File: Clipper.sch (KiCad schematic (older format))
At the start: 35 parts, among them U16 LM4562, U17 LM4562, U18 LM4562

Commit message: More components specified
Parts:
- removed U16, U17, U18: LM4562, ~, symbol LM4562
- added U15, U16: LME49740, ~, symbol LME49740
- D16, D17, D18, D19, D20, D21, D22, D23: DigiKey (none) -> 568-1360-1-ND
- gave numbers to parts that had none: 17
- renumbered C38 to C40, C39 to C41, C40 to C42, C41 to C43
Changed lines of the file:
@@
 Sheet 5 6
 Title ""
-Date "23 may 2014"
+Date "25 may 2014"
 Rev ""
 Comp ""
@@
 	-1   0    0    1
 $EndComp
-$Comp
-L LM4562 U16
-U 1 1 536E7276
-P 2500 3150
-F 0 "U16" H 2750 3000 60  0000 L CNN
-F 1 "LM4562" H 2750 2900 60  0000 L CNN
-F 2 "~" H 2600 3150 60  0000 C CNN
-F 3 "~" H 2600 3150 60  0000 C CNN
-	1    2500 3150
-	1    0    0    -1
-$EndComp
 Text HLabel 2000 3350 3    60   Input ~ 0
 AGND
@@
 F 2 "~" H 2600 2550 60  0000 C CNN
 F 3 "~" H 2600 2550 60  0000 C CNN
+F 4 "568-1360-1-ND" H 2600 2550 60  0001 C CNN "DigiKey"
 	1    2600 2550
 	1    0    0    -1
@@
 F 2 "~" H 2900 2250 60  0000 C CNN
 F 3 "~" H 2900 2250 60  0000 C CNN
+F 4 "568-1360-1-ND" H 2900 2250 60  0001 C CNN "DigiKey"
 	1    2900 2250
 	-1   0    0    -1
@@
 Text HLabel 1850 2350 0    60   Input ~ 0
 +15V
-$Comp
-L LM4562 U16
-U 2 1 536E79AB
-P 2500 5050
-F 0 "U16" H 2750 4900 60  0000 L CNN
-F 1 "LM4562" H 2750 4800 60  0000 L CNN
-F 2 "~" H 2600 5050 60  0000 C CNN
-F 3 "~" H 2600 5050 60  0000 C CNN
-	2    2500 5050
-	1    0    0    -1
-$EndComp
 Text HLabel 2000 5250 3    60   Input ~ 0
 AGND
@@
 F 2 "~" H 2600 4450 60  0000 C CNN
 F 3 "~" H 2600 4450 60  0000 C CNN
+F 4 "568-1360-1-ND" H 2600 4450 60  0001 C CNN "DigiKey"
 	1    2600 4450
 	1    0    0    -1
@@
 F 2 "~" H 2900 4150 60  0000 C CNN
 F 3 "~" H 2900 4150 60  0000 C CNN
+F 4 "568-1360-1-ND" H 2900 4150 60  0001 C CNN "DigiKey"
 	1    2900 4150
 	-1   0    0    -1
@@
 Text HLabel 1850 5650 0    60   Input ~ 0
 -15V
-$Comp
-L LM4562 U17
-U 1 1 536E7B83
-P 4650 3800
-F 0 "U17" H 4900 3650 60  0000 L CNN
-F 1 "LM4562" H 4900 3550 60  0000 L CNN
-F 2 "~" H 4750 3800 60  0000 C CNN
-F 3 "~" H 4750 3800 60  0000 C CNN
-	1    4650 3800
-	1    0    0    -1
-$EndComp
 Text HLabel 4150 4000 3    60   Input ~ 0
 AGND
@@
 Text HLabel 4650 4200 0    60   Input ~ 0
 -15V
-$Comp
-L LM4562 U17
-U 2 1 536E8363
-P 7900 3150
-F 0 "U17" H 8150 3000 60  0000 L CNN
-F 1 "LM4562" H 8150 2900 60  0000 L CNN
-F 2 "~" H 8000 3150 60  0000 C CNN
-F 3 "~" H 8000 3150 60  0000 C CNN
-	2    7900 3150
-	1    0    0    -1
-$EndComp
 Text HLabel 7400 3350 3    60   Input ~ 0
 AGND
@@
 F 2 "~" H 8000 2550 60  0000 C CNN
 F 3 "~" H 8000 2550 60  0000 C CNN
+F 4 "568-1360-1-ND" H 8000 2550 60  0001 C CNN "DigiKey"
 	1    8000 2550
 	1    0    0    -1
@@
 F 2 "~" H 8300 2250 60  0000 C CNN
 F 3 "~" H 8300 2250 60  0000 C CNN
+F 4 "568-1360-1-ND" H 8300 2250 60  0001 C CNN "DigiKey"
 	1    8300 2250
 	-1   0    0    -1
@@
 Text HLabel 7250 2350 0    60   Input ~ 0
 +15V
-$Comp
-L LM4562 U18
-U 1 1 536E839D
-P 7900 5050
-F 0 "U18" H 8150 4900 60  0000 L CNN
-F 1 "LM4562" H 8150 4800 60  0000 L CNN
-F 2 "~" H 8000 5050 60  0000 C CNN
-F 3 "~" H 8000 5050 60  0000 C CNN
-	1    7900 5050
-	1    0    0    -1
-$EndComp
 Text HLabel 7400 5250 3    60   Input ~ 0
 AGND
@@
 F 2 "~" H 8000 4450 60  0000 C CNN
 F 3 "~" H 8000 4450 60  0000 C CNN
+F 4 "568-1360-1-ND" H 8000 4450 60  0001 C CNN "DigiKey"
 	1    8000 4450
 	1    0    0    -1
@@
 F 2 "~" H 8300 4150 60  0000 C CNN
 F 3 "~" H 8300 4150 60  0000 C CNN
+F 4 "568-1360-1-ND" H 8300 4150 60  0001 C CNN "DigiKey"
 	1    8300 4150
 	-1   0    0    -1
@@
 Text HLabel 7250 5650 0    60   Input ~ 0
 -15V
-$Comp
-L LM4562 U18
-U 2 1 536E83E9
-P 10050 3800
-F 0 "U18" H 10300 3650 60  0000 L CNN
-F 1 "LM4562" H 10300 3550 60  0000 L CNN
-F 2 "~" H 10150 3800 60  0000 C CNN
-F 3 "~" H 10150 3800 60  0000 C CNN
-	2    10050 3800
-	1    0    0    -1
-$EndComp
 Text HLabel 9550 4000 3    60   Input ~ 0
 AGND
@@
 Set to clip at +/- 6.25 V
 $Comp
-L C C38
+L C C40
 U 1 1 536EC1E0
 P 5450 1700
-F 0 "C38" H 5450 1800 40  0000 L CNN
+F 0 "C40" H 5450 1800 40  0000 L CNN
 F 1 "470n" H 5456 1615 40  0000 L CNN
 F 2 "~" H 5488 1550 30  0000 C CNN
@@
 $EndComp
 $Comp
-L C C40
+L C C42
 U 1 1 537D7769
 P 5800 1700
-F 0 "C40" H 5800 1800 40  0000 L CNN
+F 0 "C42" H 5800 1800 40  0000 L CNN
 F 1 "470n" H 5806 1615 40  0000 L CNN
 F 2 "~" H 5838 1550 30  0000 C CNN
@@
 $EndComp
 $Comp
-L C C39
+L C C41
 U 1 1 537D7778
 P 5450 2100
-F 0 "C39" H 5450 2200 40  0000 L CNN
+F 0 "C41" H 5450 2200 40  0000 L CNN
 F 1 "470n" H 5456 2015 40  0000 L CNN
 F 2 "~" H 5488 1950 30  0000 C CNN
@@
 $EndComp
 $Comp
-L C C41
+L C C43
 U 1 1 537D7787
 P 5800 2100
-F 0 "C41" H 5800 2200 40  0000 L CNN
+F 0 "C43" H 5800 2200 40  0000 L CNN
 F 1 "470n" H 5806 2015 40  0000 L CNN
 F 2 "~" H 5838 1950 30  0000 C CNN
@@
 $EndComp
 $Comp
-L R R?
+L R R34
 U 1 1 537F3861
 P 1850 5400
-F 0 "R?" V 1930 5400 40  0000 C CNN
+F 0 "R34" V 1930 5400 40  0000 C CNN
 F 1 "24k" V 1857 5401 40  0000 C CNN
 F 2 "~" V 1780 5400 30  0000 C CNN
@@
 $EndComp
 $Comp
-L R R?
+L R R44
 U 1 1 537F3868
 P 7250 5400
-F 0 "R?" V 7330 5400 40  0000 C CNN
+F 0 "R44" V 7330 5400 40  0000 C CNN
 F 1 "24k" V 7257 5401 40  0000 C CNN
 F 2 "~" V 7180 5400 30  0000 C CNN
@@
 $EndComp
 $Comp
-L R R?
+L R R43
 U 1 1 537F387B
 P 7250 2600
-F 0 "R?" V 7330 2600 40  0000 C CNN
+F 0 "R43" V 7330 2600 40  0000 C CNN
 F 1 "24k" V 7257 2601 40  0000 C CNN
 F 2 "~" V 7180 2600 30  0000 C CNN
@@
 $EndComp
 $Comp
-L R R?
+L R R32
 U 1 1 537F38E5
 P 1450 4950
-F 0 "R?" V 1530 4950 40  0000 C CNN
+F 0 "R32" V 1530 4950 40  0000 C CNN
 F 1 "10k" V 1450 4950 40  0000 C CNN
 F 2 "~" V 1380 4950 30  0000 C CNN
@@
 $EndComp
 $Comp
-L R R?
+L R R42
 U 1 1 537F38EC
 P 6850 4950
-F 0 "R?" V 6930 4950 40  0000 C CNN
+F 0 "R42" V 6930 4950 40  0000 C CNN
 F 1 "10k" V 6850 4950 40  0000 C CNN
 F 2 "~" V 6780 4950 30  0000 C CNN
@@
 $EndComp
 $Comp
-L R R?
+L R R41
 U 1 1 537F38F3
 P 6850 3050
-F 0 "R?" V 6930 3050 40  0000 C CNN
+F 0 "R41" V 6930 3050 40  0000 C CNN
 F 1 "10k" V 6850 3050 40  0000 C CNN
 F 2 "~" V 6780 3050 30  0000 C CNN
@@
 $EndComp
 $Comp
-L R R?
+L R R35
 U 1 1 537F38FA
 P 2350 2250
-F 0 "R?" V 2430 2250 40  0000 C CNN
+F 0 "R35" V 2430 2250 40  0000 C CNN
 F 1 "10k" V 2350 2250 40  0000 C CNN
 F 2 "~" V 2280 2250 30  0000 C CNN
@@
 $EndComp
 $Comp
-L R R?
+L R R36
 U 1 1 537F3901
 P 2350 4150
-F 0 "R?" V 2430 4150 40  0000 C CNN
+F 0 "R36" V 2430 4150 40  0000 C CNN
 F 1 "10k" V 2350 4150 40  0000 C CNN
 F 2 "~" V 2280 4150 30  0000 C CNN
@@
 $EndComp
 $Comp
-L R R?
+L R R45
 U 1 1 537F3908
 P 7750 2250
-F 0 "R?" V 7830 2250 40  0000 C CNN
+F 0 "R45" V 7830 2250 40  0000 C CNN
 F 1 "10k" V 7750 2250 40  0000 C CNN
 F 2 "~" V 7680 2250 30  0000 C CNN
@@
 $EndComp
 $Comp
-L R R?
+L R R46
 U 1 1 537F390F
 P 7750 4150
-F 0 "R?" V 7830 4150 40  0000 C CNN
+F 0 "R46" V 7830 4150 40  0000 C CNN
 F 1 "10k" V 7750 4150 40  0000 C CNN
 F 2 "~" V 7680 4150 30  0000 C CNN
@@
 $EndComp
 $Comp
-L R R?
+L R R48
 U 1 1 537F3ABF
 P 9000 3700
-F 0 "R?" V 9080 3700 40  0000 C CNN
+F 0 "R48" V 9080 3700 40  0000 C CNN
 F 1 "2.2k" V 9007 3701 40  0000 C CNN
 F 2 "~" V 8930 3700 30  0000 C CNN
@@
 $EndComp
 $Comp
-L R R?
+L R R49
 U 1 1 537F3AC6
 P 9000 4000
-F 0 "R?" V 9080 4000 40  0000 C CNN
+F 0 "R49" V 9080 4000 40  0000 C CNN
 F 1 "2.2k" V 9007 4001 40  0000 C CNN
 F 2 "~" V 8930 4000 30  0000 C CNN
@@
 $EndComp
 $Comp
-L R R?
+L R R50
 U 1 1 537F3ACD
 P 10150 3200
-F 0 "R?" V 10230 3200 40  0000 C CNN
+F 0 "R50" V 10230 3200 40  0000 C CNN
 F 1 "2.2k" V 10157 3201 40  0000 C CNN
 F 2 "~" V 10080 3200 30  0000 C CNN
@@
 $EndComp
 $Comp
-L R R?
+L R R37
 U 1 1 537F3AD4
 P 3600 3400
-F 0 "R?" V 3680 3400 40  0000 C CNN
+F 0 "R37" V 3680 3400 40  0000 C CNN
 F 1 "2.2k" V 3607 3401 40  0000 C CNN
 F 2 "~" V 3530 3400 30  0000 C CNN
@@
 $EndComp
 $Comp
-L R R?
+L R R38
 U 1 1 537F3ADB
 P 3600 3700
-F 0 "R?" V 3680 3700 40  0000 C CNN
+F 0 "R38" V 3680 3700 40  0000 C CNN
 F 1 "2.2k" V 3607 3701 40  0000 C CNN
 F 2 "~" V 3530 3700 30  0000 C CNN
@@
 $EndComp
 $Comp
-L R R?
+L R R39
 U 1 1 537F3AE2
 P 3600 4000
-F 0 "R?" V 3680 4000 40  0000 C CNN
+F 0 "R39" V 3680 4000 40  0000 C CNN
 F 1 "2.2k" V 3607 4001 40  0000 C CNN
 F 2 "~" V 3530 4000 30  0000 C CNN
@@
 $EndComp
 $Comp
-L R R?
+L R R40
 U 1 1 537F3AE9
 P 4750 3200
-F 0 "R?" V 4830 3200 40  0000 C CNN
+F 0 "R40" V 4830 3200 40  0000 C CNN
 F 1 "2.2k" V 4757 3201 40  0000 C CNN
 F 2 "~" V 4680 3200 30  0000 C CNN
@@
 	0    -1   -1   0
 $EndComp
+$Comp
+L LME49740 U15
+U 3 1 5380327C
+P 2500 3150
+F 0 "U15" H 2750 3000 60  0000 L CNN
+F 1 "LME49740" H 2750 2900 60  0000 L CNN
+F 2 "~" H 2600 3150 60  0000 C CNN
+F 3 "~" H 2600 3150 60  0000 C CNN
+	3    2500 3150
+	1    0    0    -1
+$EndComp
+$Comp
+L LME49740 U15
+U 4 1 53803307
+P 2500 5050
+F 0 "U15" H 2750 4900 60  0000 L CNN
+F 1 "LME49740" H 2750 4800 60  0000 L CNN
+F 2 "~" H 2600 5050 60  0000 C CNN
+F 3 "~" H 2600 5050 60  0000 C CNN
+	4    2500 5050
+	1    0    0    -1
+$EndComp
+$Comp
+L LME49740 U16
+U 4 1 53803335
+P 7900 5050
+F 0 "U16" H 8150 4900 60  0000 L CNN
+F 1 "LME49740" H 8150 4800 60  0000 L CNN
+F 2 "~" H 8000 5050 60  0000 C CNN
+F 3 "~" H 8000 5050 60  0000 C CNN
+	4    7900 5050
+	1    0    0    -1
+$EndComp
+$Comp
+L LME49740 U16
+U 3 1 5380334C
+P 7900 3150
+F 0 "U16" H 8150 3000 60  0000 L CNN
+F 1 "LME49740" H 8150 2900 60  0000 L CNN
+F 2 "~" H 8000 3150 60  0000 C CNN
+F 3 "~" H 8000 3150 60  0000 C CNN
+	3    7900 3150
+	1    0    0    -1
+$EndComp
+$Comp
+L LME49740 U15
+U 2 1 538036F5
+P 4650 3800
+F 0 "U15" H 4900 3650 60  0000 L CNN
+F 1 "LME49740" H 4900 3550 60  0000 L CNN
+F 2 "~" H 4750 3800 60  0000 C CNN
+F 3 "~" H 4750 3800 60  0000 C CNN
+	2    4650 3800
+	1    0    0    -1
+$EndComp
+$Comp
+L LME49740 U16
+U 2 1 5380372A
+P 10050 3800
+F 0 "U16" H 10300 3650 60  0000 L CNN
+F 1 "LME49740" H 10300 3550 60  0000 L CNN
+F 2 "~" H 10150 3800 60  0000 C CNN
+F 3 "~" H 10150 3800 60  0000 C CNN
+	2    10050 3800
+	1    0    0    -1
+$EndComp
 $EndSCHEMATC

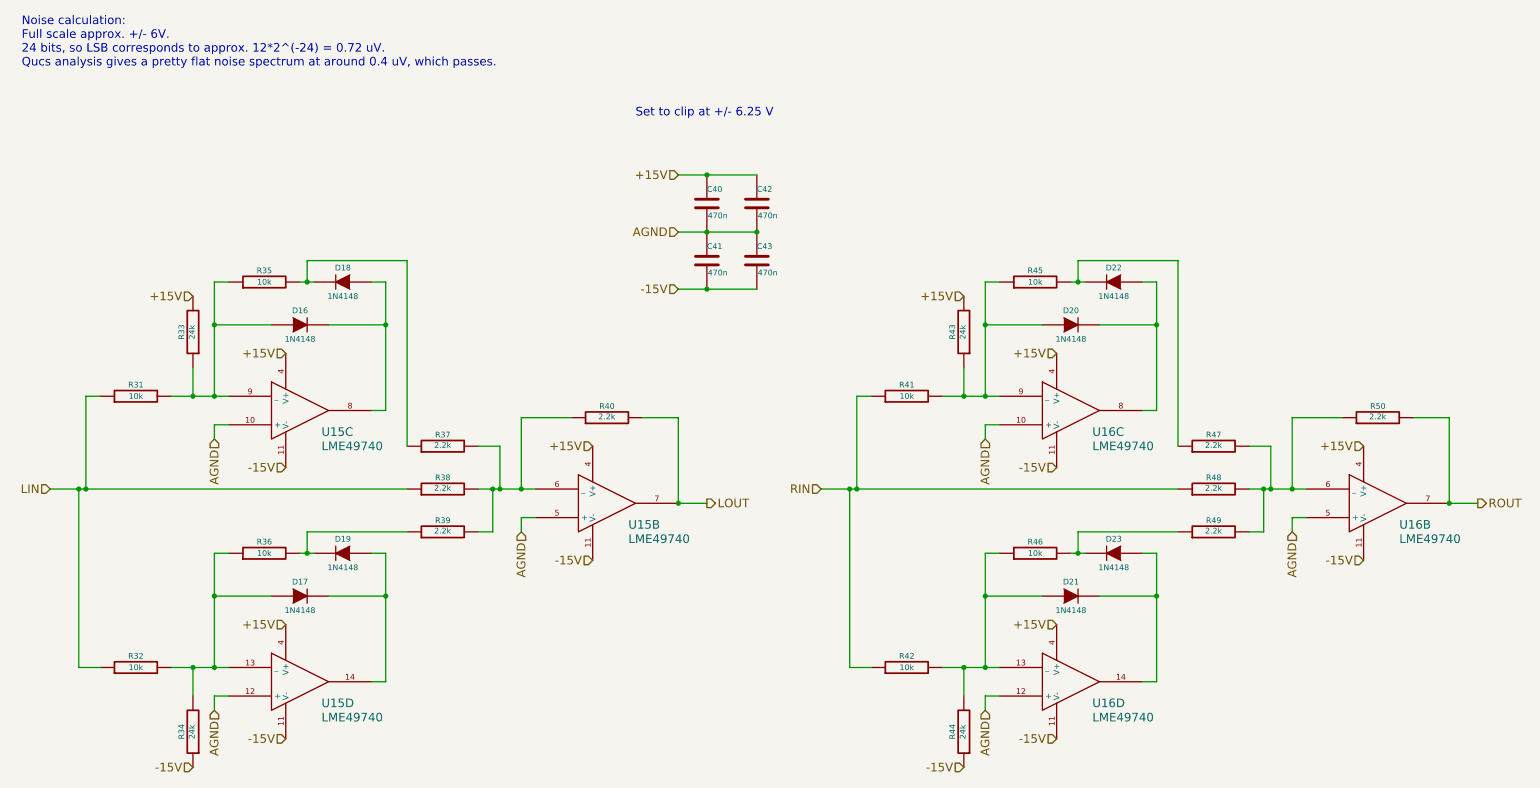
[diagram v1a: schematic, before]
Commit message: Completed component product code specification; started on footprints.
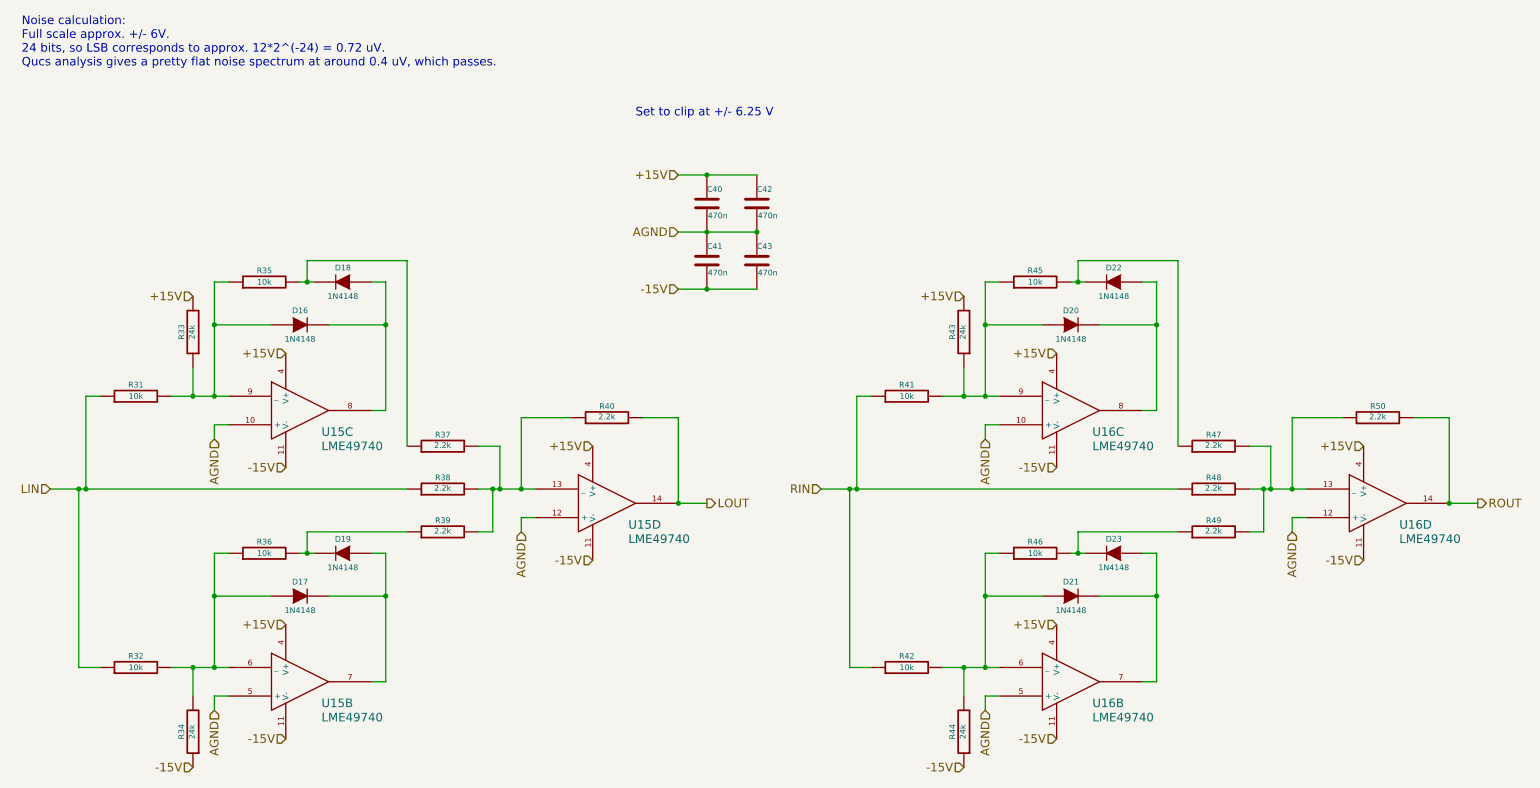
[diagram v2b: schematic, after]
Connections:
- net AGND: now also U15.12 (+), U15.5 (+), U16.12 (+), U16.5 (+); no longer U15.12 (+), U15.5 (+), U16.12 (+), U16.5 (+)
- net LOUT: now also U15.14; no longer U15.7
- net ROUT: now also U16.14; no longer U16.7
- net at D17.1 (A), R32.2, R34.2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: now also U15.6 (_); no longer U15.13 (_)
- net at D17.2 (K), D19.1 (A): now also U15.7; no longer U15.14
- net at D21.1 (A), R42.2, R44.2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: now also U16.6 (_); no longer U16.13 (_)
- net at D21.2 (K), D23.1 (A): now also U16.7; no longer U16.14
- net at R47.2, R48.2, R49.2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: now also U16.13 (_); no longer U16.6 (_)
- net at R37.2, R38.2, R39.2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: now also U15.13 (_); no longer U15.6 (_)
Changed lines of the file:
@@
 LIBS:my-conn
 LIBS:ADC-cache
-EELAYER 27 0
+EELAYER 24 0
 EELAYER END
 $Descr A4 11693 8268
@@
 $Comp
 L LME49740 U15
-U 4 1 53803307
+U 2 1 53803307
 P 2500 5050
 F 0 "U15" H 2750 4900 60  0000 L CNN
@@
 F 2 "~" H 2600 5050 60  0000 C CNN
 F 3 "~" H 2600 5050 60  0000 C CNN
-	4    2500 5050
+	2    2500 5050
 	1    0    0    -1
 $EndComp
 $Comp
 L LME49740 U16
-U 4 1 53803335
+U 2 1 53803335
 P 7900 5050
 F 0 "U16" H 8150 4900 60  0000 L CNN
@@
 F 2 "~" H 8000 5050 60  0000 C CNN
 F 3 "~" H 8000 5050 60  0000 C CNN
-	4    7900 5050
+	2    7900 5050
 	1    0    0    -1
 $EndComp
@@
 $Comp
 L LME49740 U15
-U 2 1 538036F5
+U 4 1 538036F5
 P 4650 3800
 F 0 "U15" H 4900 3650 60  0000 L CNN
@@
 F 2 "~" H 4750 3800 60  0000 C CNN
 F 3 "~" H 4750 3800 60  0000 C CNN
-	2    4650 3800
+	4    4650 3800
 	1    0    0    -1
 $EndComp
 $Comp
 L LME49740 U16
-U 2 1 5380372A
+U 4 1 5380372A
 P 10050 3800
 F 0 "U16" H 10300 3650 60  0000 L CNN
@@
 F 2 "~" H 10150 3800 60  0000 C CNN
 F 3 "~" H 10150 3800 60  0000 C CNN
-	2    10050 3800
-	1    0    0    -1
-$EndComp
+	4    10050 3800
+	1    0    0    -1
+$EndComp

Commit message: More footprint specification and connector additions; almost done.
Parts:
- C40, C41, C42, C43: footprint ~ -> Capacitors_ThroughHole:Capacitor3MMDiscRM2.5
- D16, D17, D18, D19, D20, D21, D22, D23: footprint ~ -> Diodes_ThroughHole:Diode_DO-35_SOD27_Horizontal_RM10
- R31, R32, R33, R34, R35, R36, R37, R38, R39, R40, R41, R42, R43, R44, R45, R46, R47, R48, R49, R50: footprint ~ -> Resistors_ThroughHole:Resistor_Horizontal_RM10mm
- U15, U16: footprint ~ -> Sockets_DIP:DIP-14__300_ELL
